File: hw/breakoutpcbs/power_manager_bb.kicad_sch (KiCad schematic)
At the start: 8 parts, among them IC1 LTC2943IDD#TRPBF, J1 Conn_01x05, J2 Conn_01x05, U1 INA219BxDCN

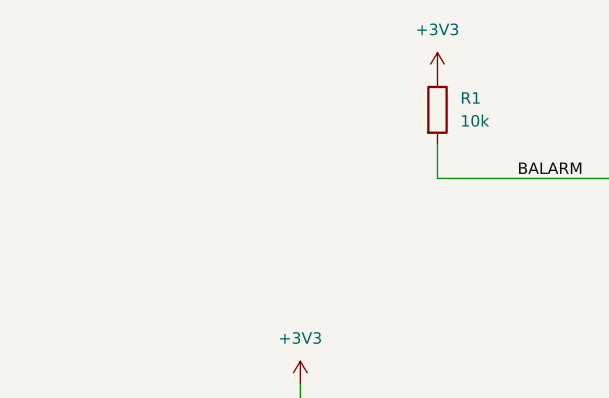
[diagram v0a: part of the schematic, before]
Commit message: new todos, the charging signal removed, plugged signal used instead
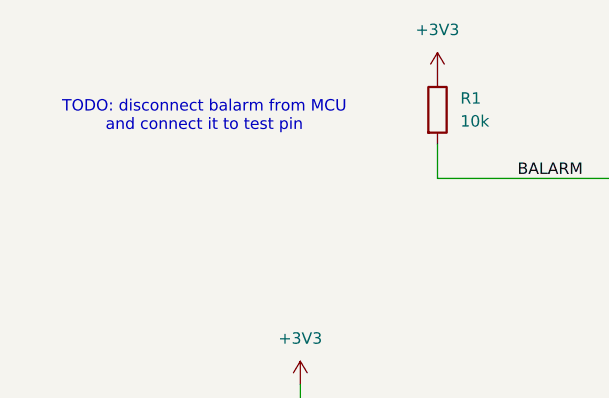
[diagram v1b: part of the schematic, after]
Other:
- note added: "TODO: disconnect balarm from MCU and connect it to test pin"
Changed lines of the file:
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@@
+		)
+	)
+	(text "TODO: disconnect balarm from MCU\nand connect it to test pin"
+		(exclude_from_sim no)
+		(at 71.882 46.482 0)
+		(effects
+			(font
+				(size 1.27 1.27)
+			)
 		)
 	)

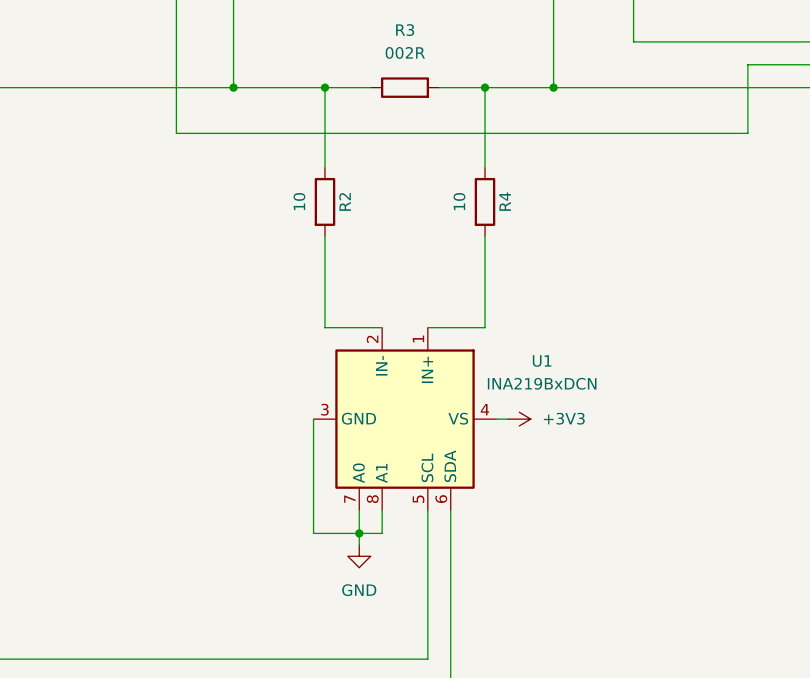
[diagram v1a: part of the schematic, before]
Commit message: updated breakoutboards components attributes
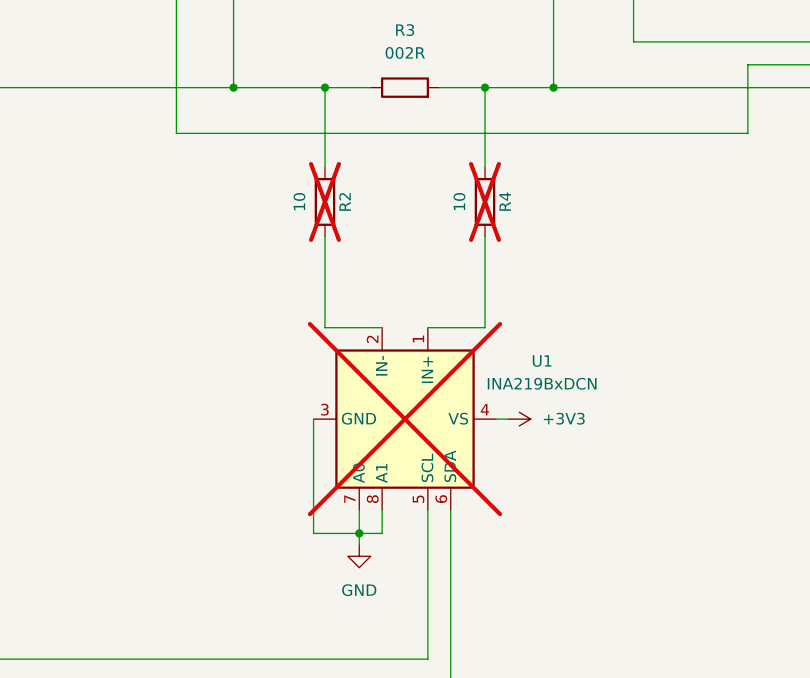
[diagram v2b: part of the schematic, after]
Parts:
- R2, R4, U1: now not fitted
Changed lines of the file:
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@@
 		(in_bom yes)
 		(on_board yes)
-		(dnp no)
+		(dnp yes)
 		(property "Reference" "R2"
 			(at 143.256 95.25 90)
@@
 		(in_bom yes)
 		(on_board yes)
-		(dnp no)
+		(dnp yes)
 		(property "Reference" "R4"
 			(at 161.036 95.25 90)
@@
 		(in_bom yes)
 		(on_board yes)
-		(dnp no)
+		(dnp yes)
 		(fields_autoplaced yes)
 		(property "Reference" "U1"
